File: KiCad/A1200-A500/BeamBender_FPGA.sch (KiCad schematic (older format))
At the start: 1 part, among them U2 GW1NR-UV9LQ144P

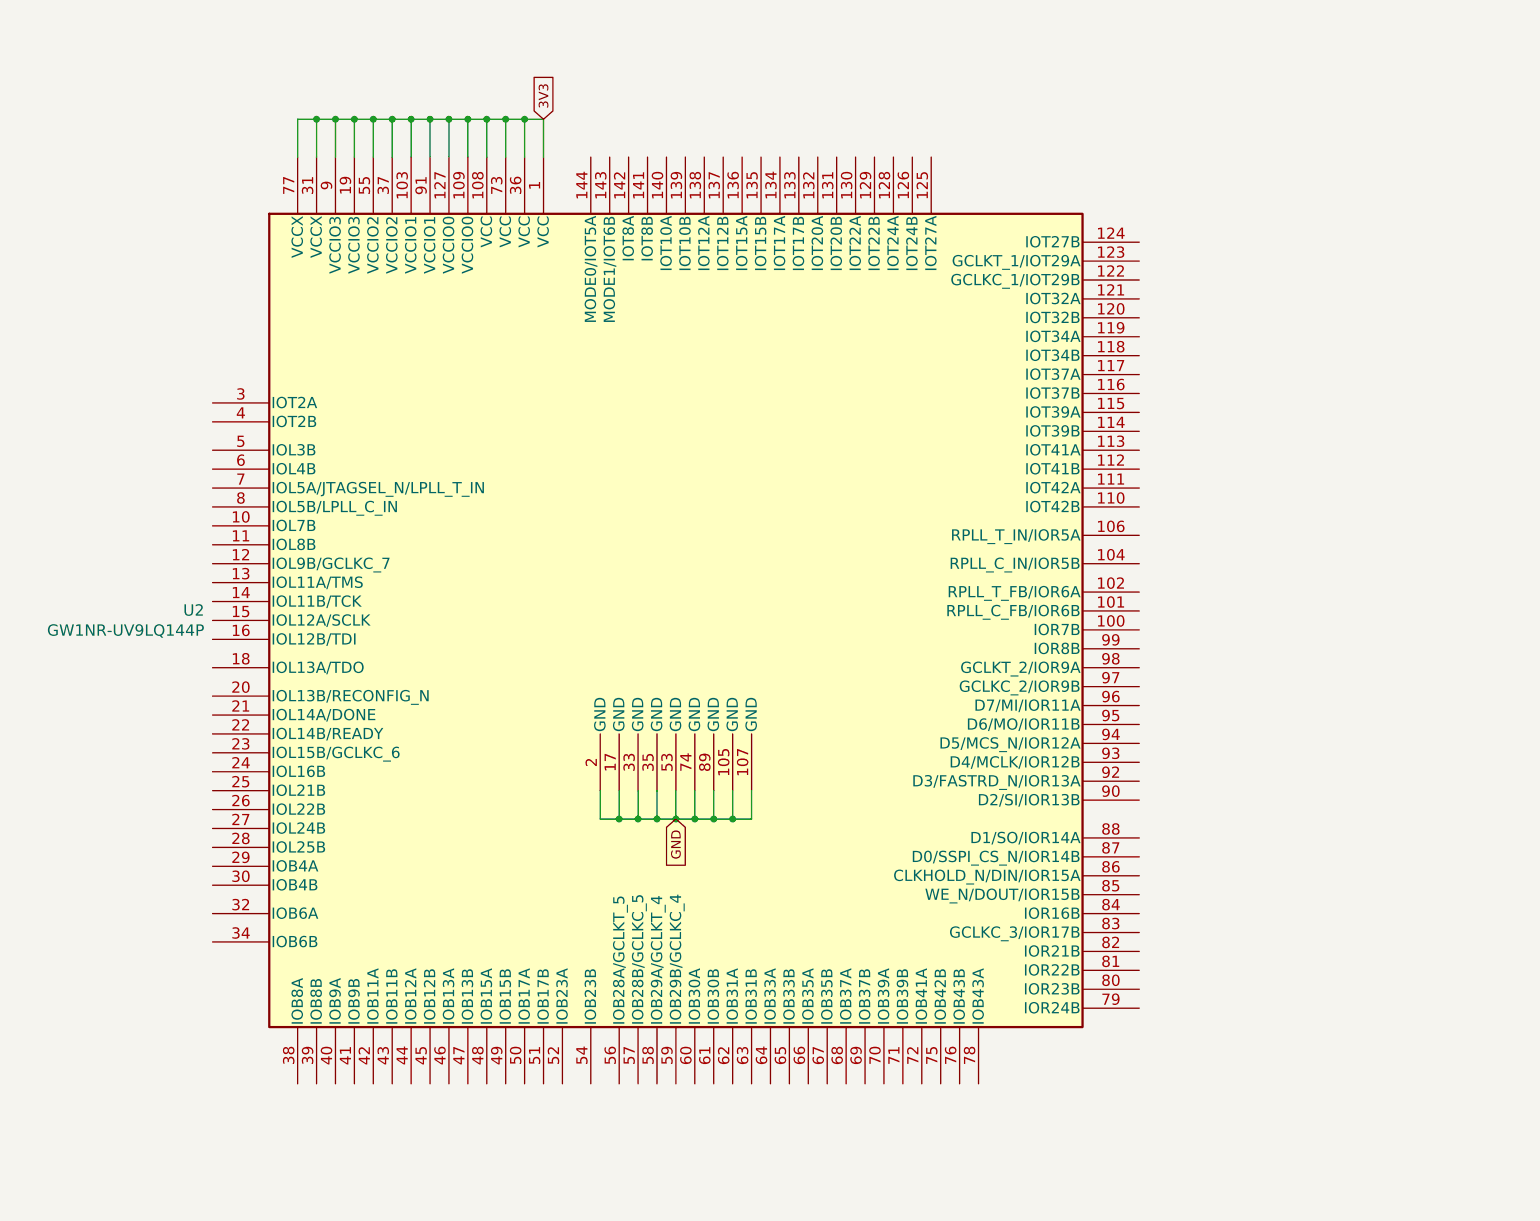
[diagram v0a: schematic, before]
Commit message: Added 27 MHz crystal oscillator X1 to GCLKT_4 pin and did some routing
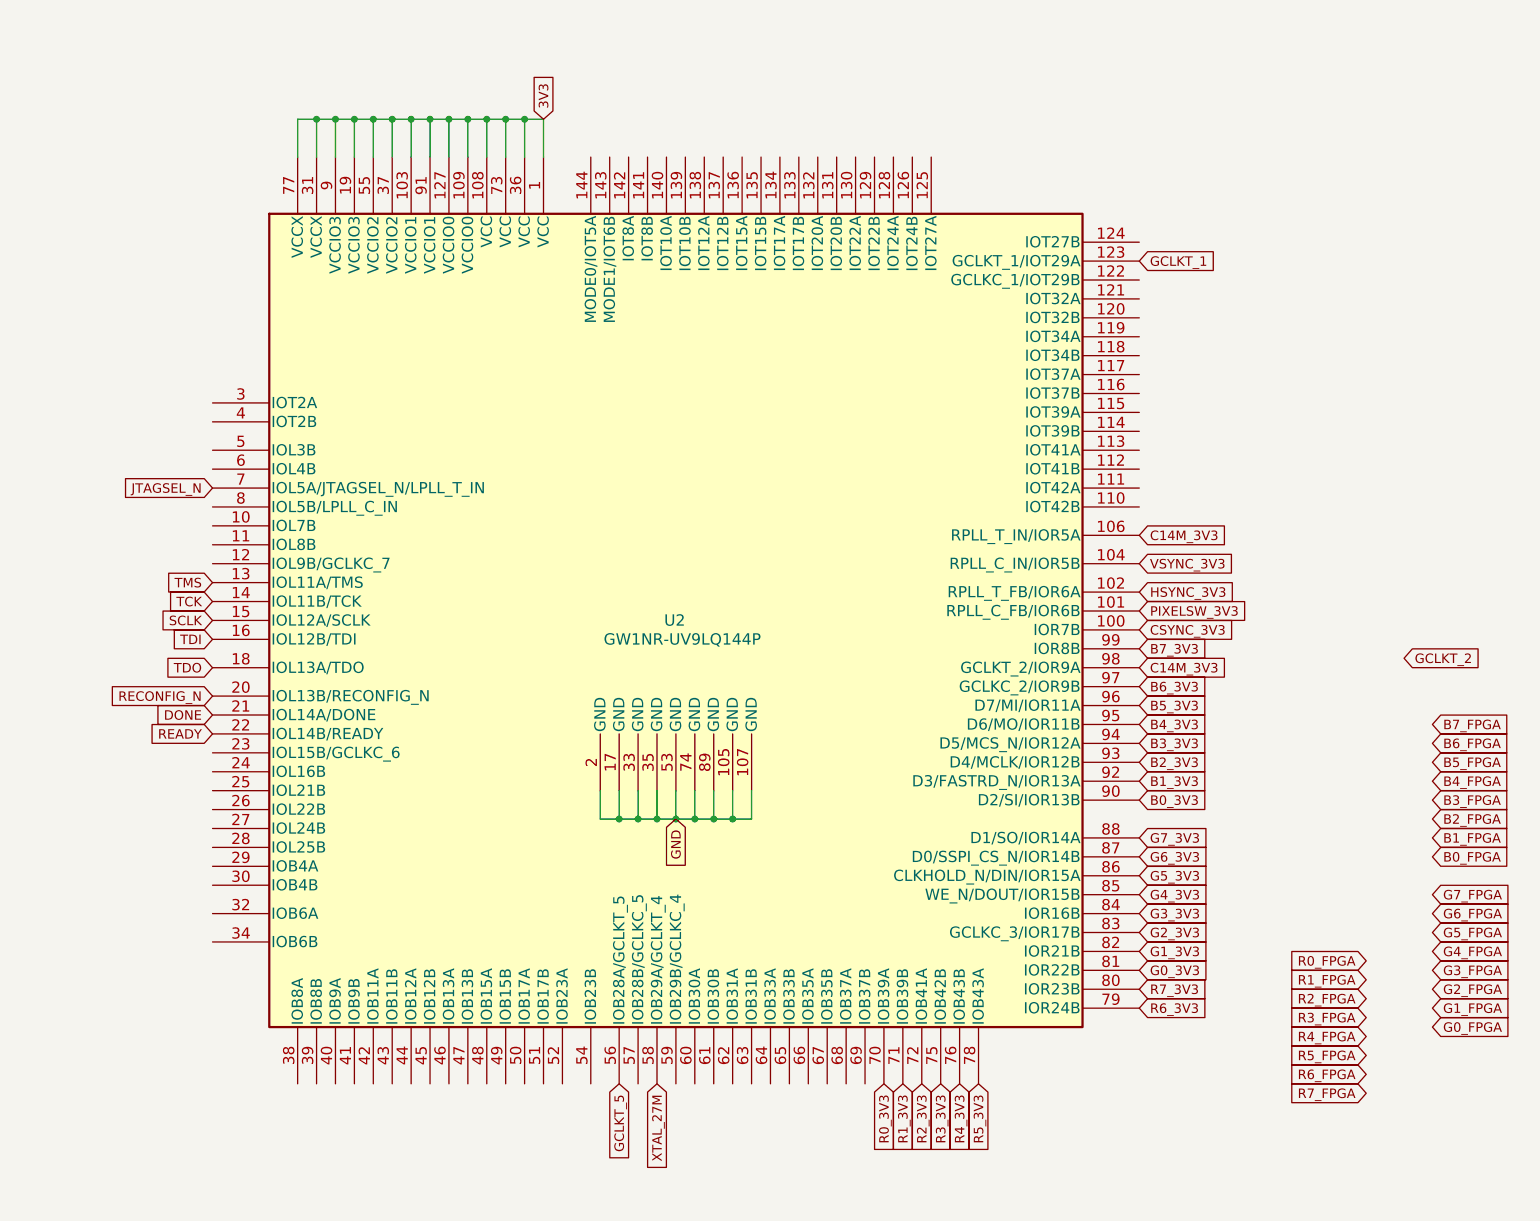
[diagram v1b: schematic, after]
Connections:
- net CSYNC_3V3: now reaches U2.100 (IOR7B)
- net PIXELSW_3V3: now reaches U2.101 (RPLL_C_FB/IOR6B)
- net HSYNC_3V3: now reaches U2.102 (RPLL_T_FB/IOR6A)
- net VSYNC_3V3: now reaches U2.104 (RPLL_C_IN/IOR5B)
- net C14M_3V3: now reaches U2.106 (RPLL_T_IN/IOR5A)
- net C14M_3V3: now also U2.98 (GCLKT_2/IOR9A)
- net GCLKT_1: now reaches U2.123 (GCLKT_1/IOT29A)
- net TMS: now reaches U2.13 (IOL11A/TMS)
- net TCK: now reaches U2.14 (IOL11B/TCK)
- net SCLK: now reaches U2.15 (IOL12A/SCLK)
- net TDI: now reaches U2.16 (IOL12B/TDI)
- net TDO: now reaches U2.18 (IOL13A/TDO)
- net RECONFIG_N: now reaches U2.20 (IOL13B/RECONFIG_N)
- net DONE: now reaches U2.21 (IOL14A/DONE)
- net READY: now reaches U2.22 (IOL14B/READY)
- net GCLKT_5: now reaches U2.56 (IOB28A/GCLKT_5)
- net XTAL_27M: now reaches U2.58 (IOB29A/GCLKT_4)
- net JTAGSEL_N: now reaches U2.7 (IOL5A/JTAGSEL_N/LPLL_T_IN)
- net R0_3V3: now reaches U2.70 (IOB39A)
- net R1_3V3: now reaches U2.71 (IOB39B)
- net R2_3V3: now reaches U2.72 (IOB41A)
- net R3_3V3: now reaches U2.75 (IOB42B)
- net R4_3V3: now reaches U2.76 (IOB43B)
- net R5_3V3: now reaches U2.78 (IOB43A)
- net R6_3V3: now reaches U2.79 (IOR24B)
- net R7_3V3: now reaches U2.80 (IOR23B)
- net G0_3V3: now reaches U2.81 (IOR22B)
- net G1_3V3: now reaches U2.82 (IOR21B)
- net G2_3V3: now reaches U2.83 (GCLKC_3/IOR17B)
- net G3_3V3: now reaches U2.84 (IOR16B)
- net G4_3V3: now reaches U2.85 (WE_N/DOUT/IOR15B)
- net G5_3V3: now reaches U2.86 (CLKHOLD_N/DIN/IOR15A)
- net G6_3V3: now reaches U2.87 (D0/SSPI_CS_N/IOR14B)
- net G7_3V3: now reaches U2.88 (D1/SO/IOR14A)
- net B0_3V3: now reaches U2.90 (D2/SI/IOR13B)
- net B1_3V3: now reaches U2.92 (D3/FASTRD_N/IOR13A)
- net B2_3V3: now reaches U2.93 (D4/MCLK/IOR12B)
- net B3_3V3: now reaches U2.94 (D5/MCS_N/IOR12A)
- net B4_3V3: now reaches U2.95 (D6/MO/IOR11B)
- net B5_3V3: now reaches U2.96 (D7/MI/IOR11A)
- net B6_3V3: now reaches U2.97 (GCLKC_2/IOR9B)
- net B7_3V3: now reaches U2.99 (IOR8B)
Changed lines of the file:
@@
 U 1 1 65457DDB
 P 4050 3700
-F 0 "U2" H 1557 3753 60  0000 R CNN
-F 1 "GW1NR-UV9LQ144P" H 1557 3647 60  0000 R CNN
+F 0 "U2" H 4100 3700 60  0000 R CNN
+F 1 "GW1NR-UV9LQ144P" H 4500 3600 60  0000 R CNN
 F 2 "Package_QFP:LQFP-144_20x20mm_P0.5mm" H 4050 3800 60  0001 C CNN
 F 3 "" H 5500 4900 60  0001 C CNN
@@
 Wire Wire Line
 	3250 1050 3350 1050
+Text GLabel 1600 3500 0    50   Input ~ 0
+TMS
+Text GLabel 1600 3600 0    50   Input ~ 0
+TCK
+Text GLabel 1600 3700 0    50   Input ~ 0
+SCLK
+Text GLabel 1600 3800 0    50   Input ~ 0
+TDI
+Text GLabel 1600 3950 0    50   Input ~ 0
+TDO
+Text GLabel 1600 4100 0    50   Input ~ 0
+RECONFIG_N
+Text GLabel 1600 4200 0    50   Input ~ 0
+DONE
+Text GLabel 1600 4300 0    50   Input ~ 0
+READY
+Text GLabel 6500 1800 2    50   Input ~ 0
+GCLKT_1
+Text GLabel 7900 3900 2    50   Input ~ 0
+GCLKT_2
+Text GLabel 3750 6150 3    50   Input ~ 0
+GCLKT_5
+Text GLabel 1600 3000 0    50   Input ~ 0
+JTAGSEL_N
+Text GLabel 6500 3750 2    50   Input ~ 0
+CSYNC_3V3
+Text GLabel 6500 3650 2    50   Input ~ 0
+PIXELSW_3V3
+Text GLabel 6500 3250 2    50   Input ~ 0
+C14M_3V3
+Text GLabel 6500 3400 2    50   Input ~ 0
+VSYNC_3V3
+Text GLabel 6500 3550 2    50   Input ~ 0
+HSYNC_3V3
+Text GLabel 6500 3950 2    50   Input ~ 0
+C14M_3V3
+Text GLabel 8050 4950 2    50   Input ~ 0
+B0_FPGA
+Text GLabel 8050 4850 2    50   Input ~ 0
+B1_FPGA
+Text GLabel 8050 4750 2    50   Input ~ 0
+B2_FPGA
+Text GLabel 8050 4650 2    50   Input ~ 0
+B3_FPGA
+Text GLabel 8050 4550 2    50   Input ~ 0
+B4_FPGA
+Text GLabel 8050 4450 2    50   Input ~ 0
+B5_FPGA
+Text GLabel 8050 4350 2    50   Input ~ 0
+B6_FPGA
+Text GLabel 8050 4250 2    50   Input ~ 0
+B7_FPGA
+Text GLabel 8050 5850 2    50   Input ~ 0
+G0_FPGA
+Text GLabel 8050 5750 2    50   Input ~ 0
+G1_FPGA
+Text GLabel 8050 5650 2    50   Input ~ 0
+G2_FPGA
+Text GLabel 8050 5550 2    50   Input ~ 0
+G3_FPGA
+Text GLabel 8050 5450 2    50   Input ~ 0
+G4_FPGA
+Text GLabel 8050 5350 2    50   Input ~ 0
+G5_FPGA
+Text GLabel 8050 5250 2    50   Input ~ 0
+G6_FPGA
+Text GLabel 8050 5150 2    50   Input ~ 0
+G7_FPGA
+Text GLabel 7700 5500 0    50   Input ~ 0
+R0_FPGA
+Text GLabel 7700 5600 0    50   Input ~ 0
+R1_FPGA
+Text GLabel 7700 5700 0    50   Input ~ 0
+R2_FPGA
+Text GLabel 7700 5800 0    50   Input ~ 0
+R3_FPGA
+Text GLabel 7700 5900 0    50   Input ~ 0
+R4_FPGA
+Text GLabel 7700 6000 0    50   Input ~ 0
+R5_FPGA
+Text GLabel 7700 6100 0    50   Input ~ 0
+R6_FPGA
+Text GLabel 7700 6200 0    50   Input ~ 0
+R7_FPGA
+Text GLabel 5150 6150 3    50   Input ~ 0
+R0_3V3
+Text GLabel 5250 6150 3    50   Input ~ 0
+R1_3V3
+Text GLabel 5350 6150 3    50   Input ~ 0
+R2_3V3
+Text GLabel 5450 6150 3    50   Input ~ 0
+R3_3V3
+Text GLabel 6500 4650 2    50   Input ~ 0
+B0_3V3
+Text GLabel 6500 4550 2    50   Input ~ 0
+B1_3V3
+Text GLabel 6500 4450 2    50   Input ~ 0
+B2_3V3
+Text GLabel 6500 4350 2    50   Input ~ 0
+B3_3V3
+Text GLabel 6500 5250 2    50   Input ~ 0
+G3_3V3
+Text GLabel 6500 5350 2    50   Input ~ 0
+G2_3V3
+Text GLabel 6500 5450 2    50   Input ~ 0
+G1_3V3
+Text GLabel 6500 5550 2    50   Input ~ 0
+G0_3V3
+Text GLabel 6500 4250 2    50   Input ~ 0
+B4_3V3
+Text GLabel 6500 4150 2    50   Input ~ 0
+B5_3V3
+Text GLabel 6500 4050 2    50   Input ~ 0
+B6_3V3
+Text GLabel 6500 3850 2    50   Input ~ 0
+B7_3V3
+Text GLabel 6500 5150 2    50   Input ~ 0
+G4_3V3
+Text GLabel 6500 5050 2    50   Input ~ 0
+G5_3V3
+Text GLabel 6500 4950 2    50   Input ~ 0
+G6_3V3
+Text GLabel 6500 4850 2    50   Input ~ 0
+G7_3V3
+Text GLabel 5550 6150 3    50   Input ~ 0
+R4_3V3
+Text GLabel 5650 6150 3    50   Input ~ 0
+R5_3V3
+Text GLabel 6500 5750 2    50   Input ~ 0
+R6_3V3
+Text GLabel 6500 5650 2    50   Input ~ 0
+R7_3V3
+Text GLabel 3950 6150 3    50   Input ~ 0
+XTAL_27M
 $EndSCHEMATC

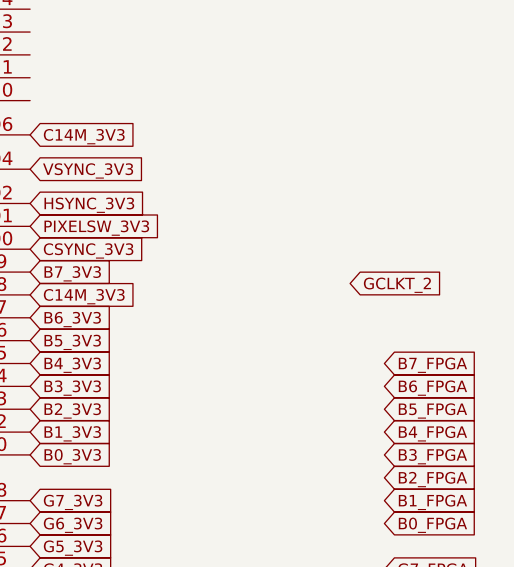
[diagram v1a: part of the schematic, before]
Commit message: Changed to four layer stackup, added some caps and done some more routing
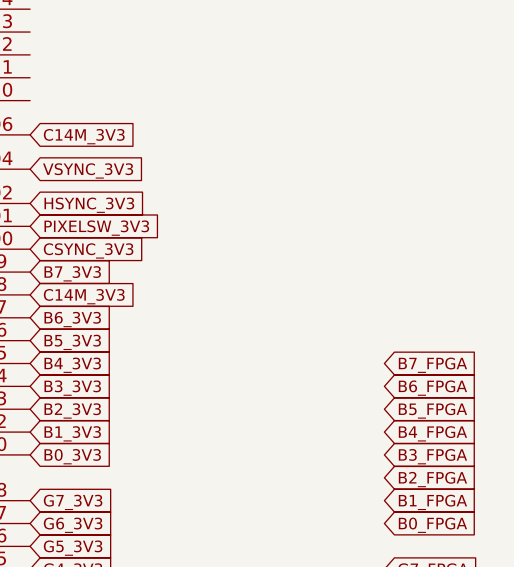
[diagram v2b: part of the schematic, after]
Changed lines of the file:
@@
 Text GLabel 6500 1800 2    50   Input ~ 0
 GCLKT_1
-Text GLabel 7900 3900 2    50   Input ~ 0
-GCLKT_2
 Text GLabel 3750 6150 3    50   Input ~ 0
 GCLKT_5

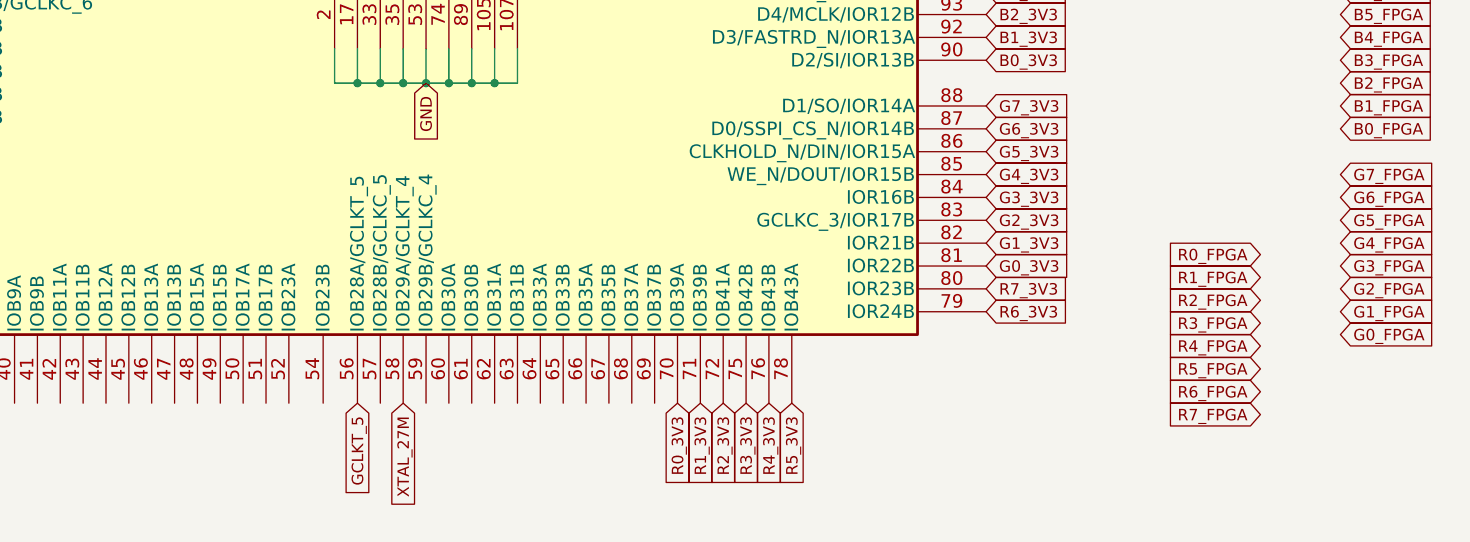
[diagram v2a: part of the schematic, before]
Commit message: more place and route done
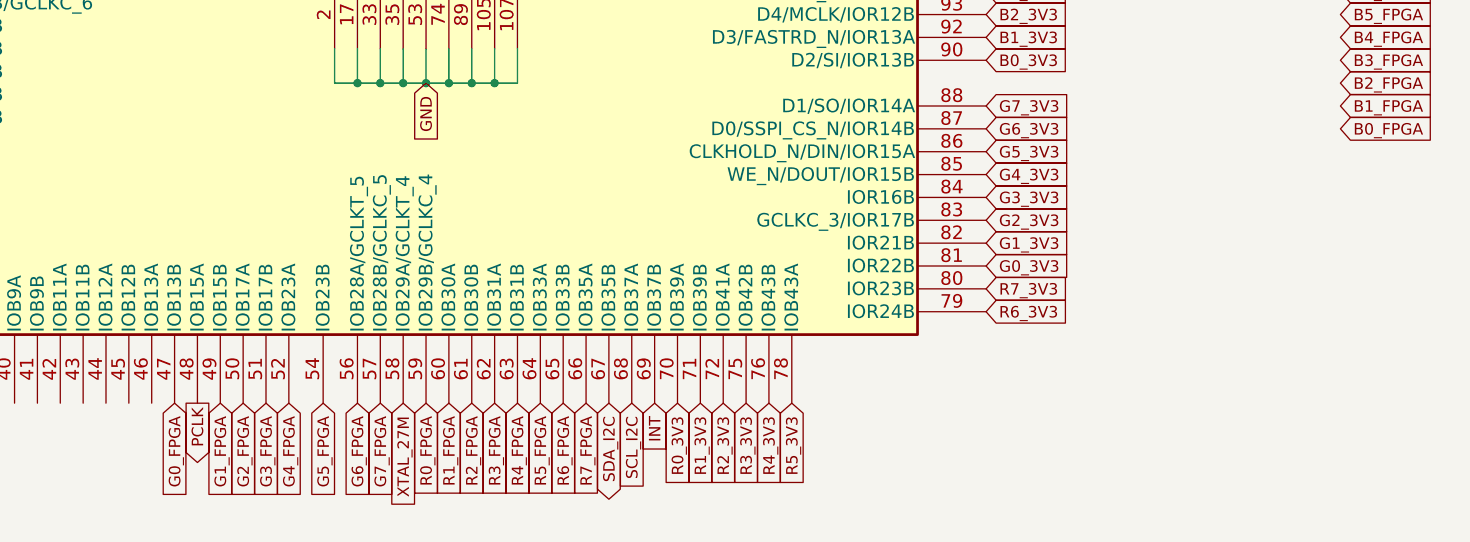
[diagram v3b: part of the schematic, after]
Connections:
- net GCLKT_5 is gone; now on net G6_FPGA: U2.56 (IOB28A/GCLKT_5)
- net G0_FPGA: now also U2.47 (IOB13B)
- net G1_FPGA: now also U2.49 (IOB15B)
- net G2_FPGA: now also U2.50 (IOB17A)
- net G3_FPGA: now also U2.51 (IOB17B)
- net G4_FPGA: now also U2.52 (IOB23A)
- net G5_FPGA: now also U2.54 (IOB23B)
- net G7_FPGA: now also U2.57 (IOB28B/GCLKC_5)
- net R0_FPGA: now also U2.59 (IOB29B/GCLKC_4)
- net R1_FPGA: now also U2.60 (IOB30A)
- net R2_FPGA: now also U2.61 (IOB30B)
- net R3_FPGA: now also U2.62 (IOB31A)
- net R4_FPGA: now also U2.63 (IOB31B)
- net R5_FPGA: now also U2.64 (IOB33A)
- net R6_FPGA: now also U2.65 (IOB33B)
- net R7_FPGA: now also U2.66 (IOB35A)
- net PCLK: now reaches U2.48 (IOB15A)
- net SDA_I2C: now reaches U2.67 (IOB35B)
- net SCL_I2C: now reaches U2.68 (IOB37A)
- net INT: now reaches U2.69 (IOB37B)
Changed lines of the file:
@@
 Text GLabel 6500 1800 2    50   Input ~ 0
 GCLKT_1
-Text GLabel 3750 6150 3    50   Input ~ 0
-GCLKT_5
+Text GLabel 3050 6150 3    50   Output ~ 0
+PCLK
 Text GLabel 1600 3000 0    50   Input ~ 0
 JTAGSEL_N
@@
 Text GLabel 8050 4250 2    50   Input ~ 0
 B7_FPGA
-Text GLabel 8050 5850 2    50   Input ~ 0
+Text GLabel 2950 6150 3    50   Input ~ 0
 G0_FPGA
-Text GLabel 8050 5750 2    50   Input ~ 0
+Text GLabel 3150 6150 3    50   Input ~ 0
 G1_FPGA
-Text GLabel 8050 5650 2    50   Input ~ 0
+Text GLabel 3250 6150 3    50   Input ~ 0
 G2_FPGA
-Text GLabel 8050 5550 2    50   Input ~ 0
+Text GLabel 3350 6150 3    50   Input ~ 0
 G3_FPGA
-Text GLabel 8050 5450 2    50   Input ~ 0
+Text GLabel 3450 6150 3    50   Input ~ 0
 G4_FPGA
-Text GLabel 8050 5350 2    50   Input ~ 0
+Text GLabel 3600 6150 3    50   Input ~ 0
 G5_FPGA
-Text GLabel 8050 5250 2    50   Input ~ 0
+Text GLabel 3750 6150 3    50   Input ~ 0
 G6_FPGA
-Text GLabel 8050 5150 2    50   Input ~ 0
+Text GLabel 3850 6150 3    50   Input ~ 0
 G7_FPGA
-Text GLabel 7700 5500 0    50   Input ~ 0
+Text GLabel 4050 6150 3    50   Input ~ 0
 R0_FPGA
-Text GLabel 7700 5600 0    50   Input ~ 0
+Text GLabel 4150 6150 3    50   Input ~ 0
 R1_FPGA
-Text GLabel 7700 5700 0    50   Input ~ 0
+Text GLabel 4250 6150 3    50   Input ~ 0
 R2_FPGA
-Text GLabel 7700 5800 0    50   Input ~ 0
+Text GLabel 4350 6150 3    50   Input ~ 0
 R3_FPGA
-Text GLabel 7700 5900 0    50   Input ~ 0
+Text GLabel 4450 6150 3    50   Input ~ 0
 R4_FPGA
-Text GLabel 7700 6000 0    50   Input ~ 0
+Text GLabel 4550 6150 3    50   Input ~ 0
 R5_FPGA
-Text GLabel 7700 6100 0    50   Input ~ 0
+Text GLabel 4650 6150 3    50   Input ~ 0
 R6_FPGA
-Text GLabel 7700 6200 0    50   Input ~ 0
+Text GLabel 4750 6150 3    50   Input ~ 0
 R7_FPGA
 Text GLabel 5150 6150 3    50   Input ~ 0
@@
 Text GLabel 3950 6150 3    50   Input ~ 0
 XTAL_27M
+Text GLabel 4950 6150 3    50   Input ~ 0
+SCL_I2C
+Text GLabel 4850 6150 3    50   BiDi ~ 0
+SDA_I2C
+Text GLabel 5050 6150 3    50   Input ~ 0
+INT
 $EndSCHEMATC
